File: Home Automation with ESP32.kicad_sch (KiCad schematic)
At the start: 26 parts, among them J1 Conn_01x04_Pin, J1 PR13-5V-450-1C, J2 Screw_Terminal_01x04, J3 Screw_Terminal_01x03, K1 RAYEX-L90AS, Q1 S8050, Q2 S8050, SW1 SW_Push, SW2 SW_Push, U1 ESP32-WROOM-32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

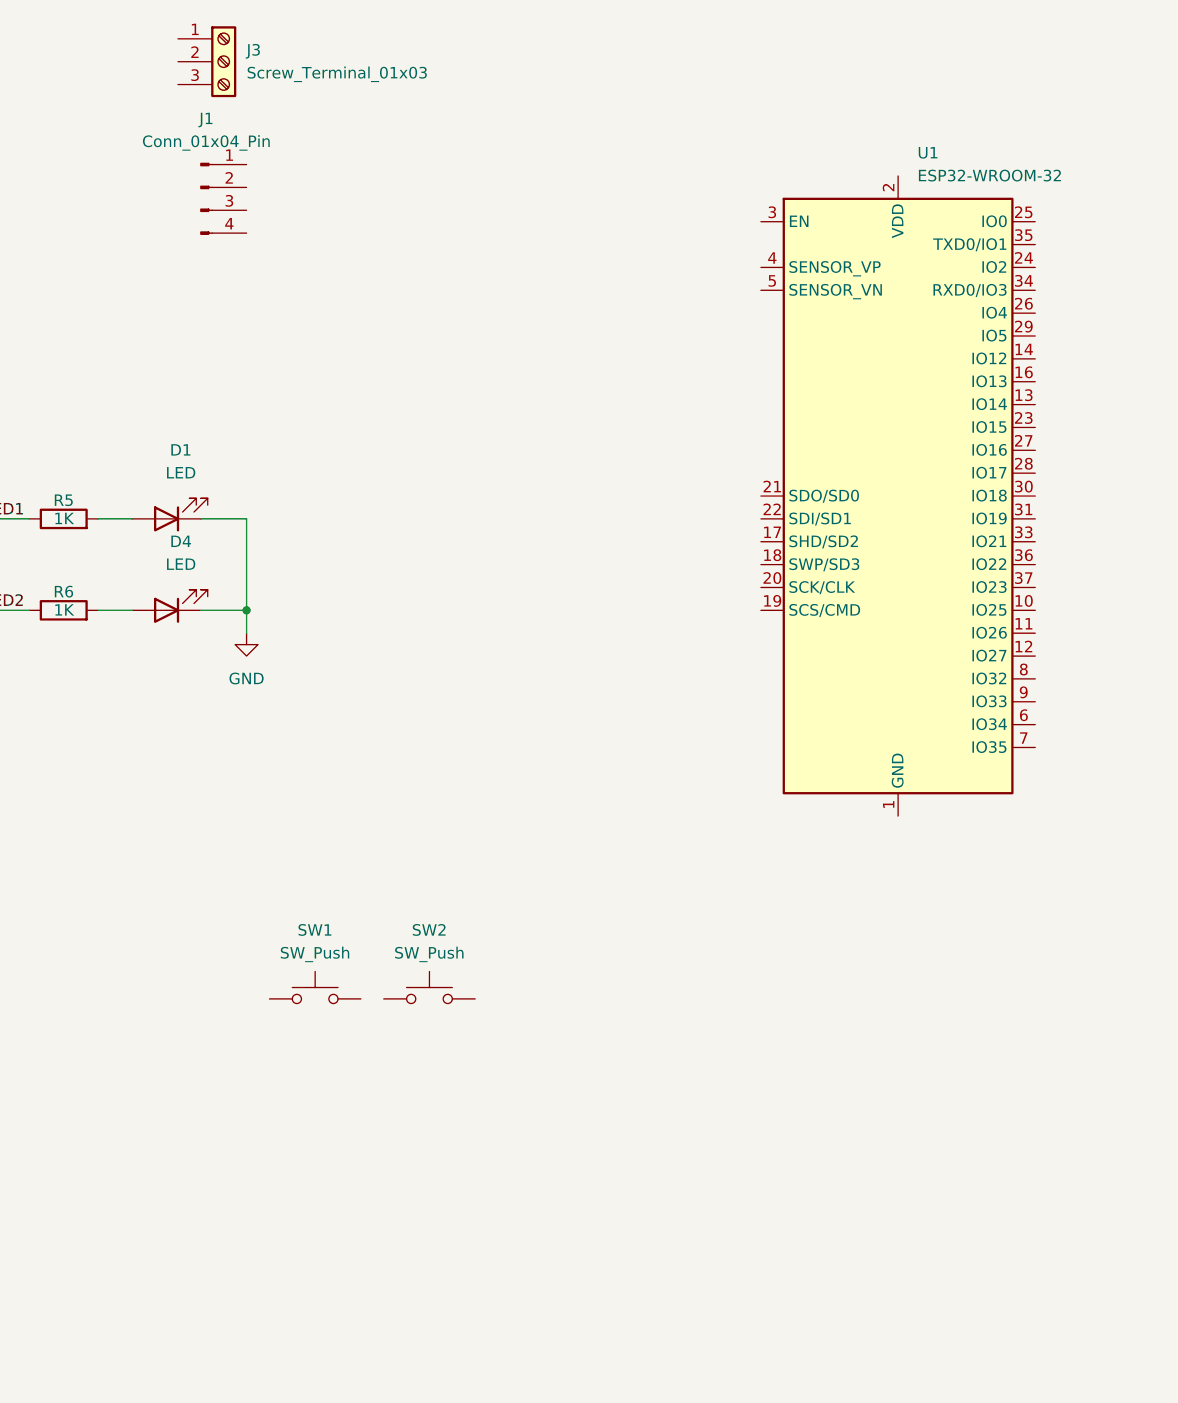
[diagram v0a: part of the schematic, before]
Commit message: Schematic Connection completed for Switches
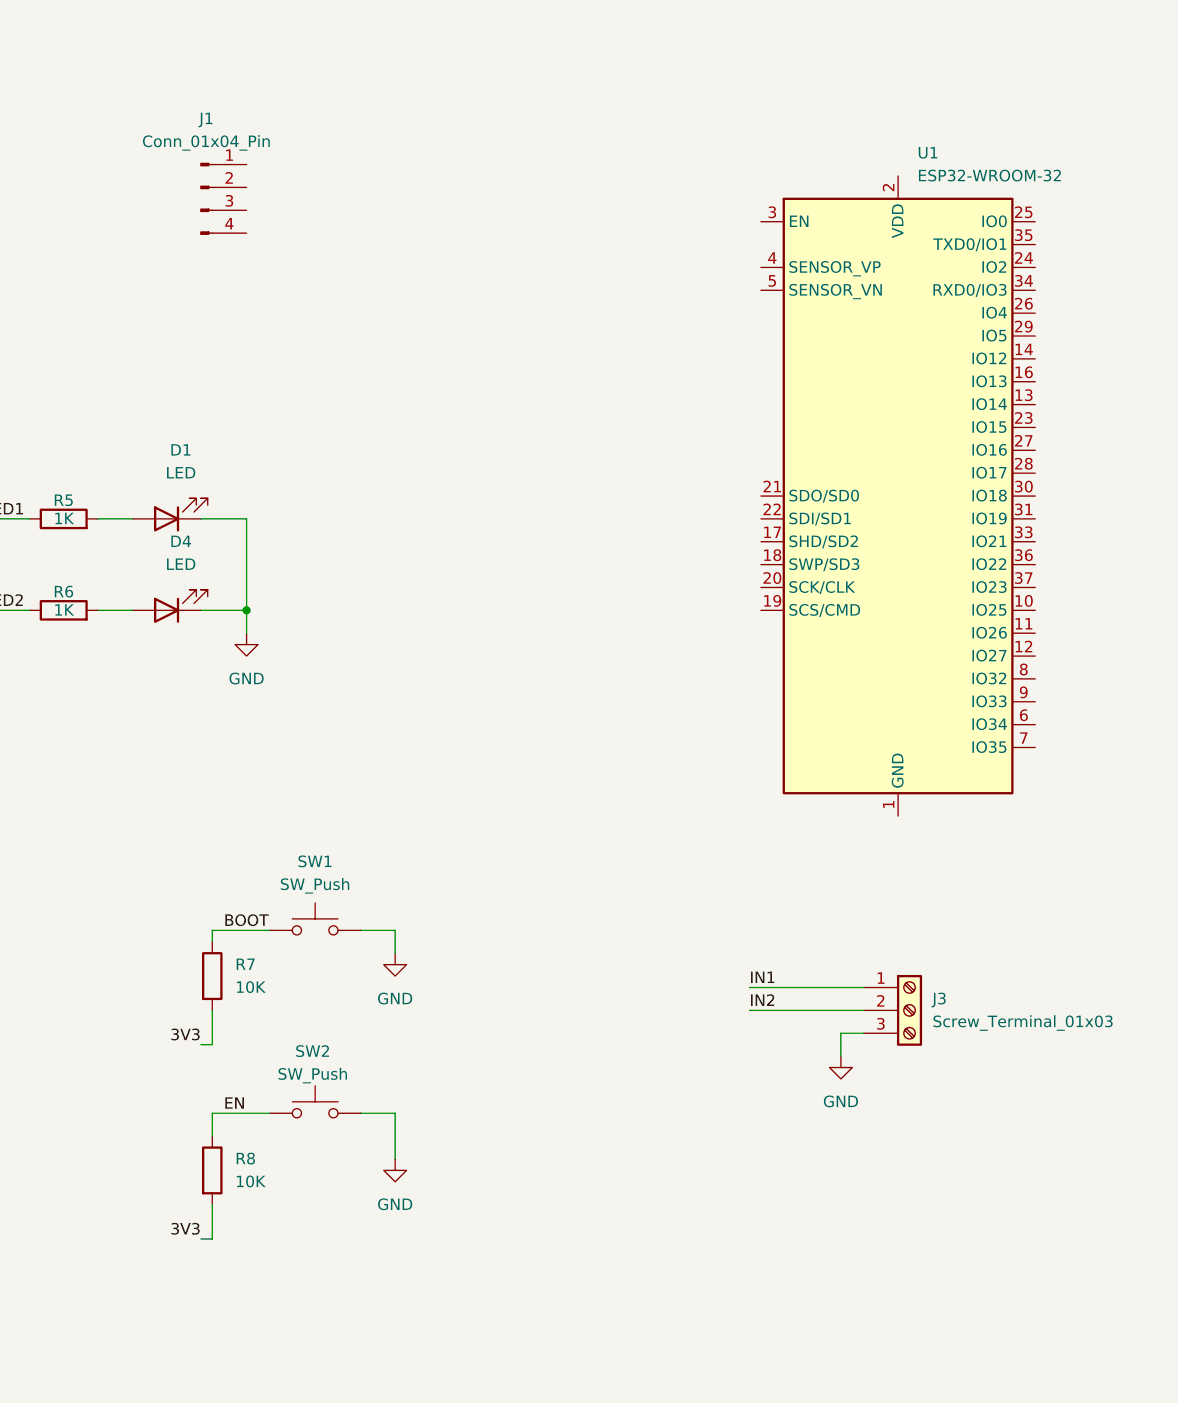
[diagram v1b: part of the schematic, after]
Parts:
- added R7, R8: 10K, symbol Device:R
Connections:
- net 3V3: now also R7.2, R8.2
- net GND: now also J3.3 (Pin_3), SW1.2, SW2.2
- net BOOT: now reaches SW1.1
- net BOOT: now also R7.1
- net EN: now reaches SW2.1
- net EN: now also R8.1
- net IN1: now reaches J3.1 (Pin_1)
- net IN2: now reaches J3.2 (Pin_2)
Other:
- moved on the sheet: J3, SW1, SW2

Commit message: Schematic Connection completed for UART
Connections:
- net 3V3: now also J1.4 (Pin_4)
- net GND: now also J1.3 (Pin_3)
- net TXD: now reaches J1.1 (Pin_1)
- net RXD: now reaches J1.2 (Pin_2)
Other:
- moved on the sheet: J1
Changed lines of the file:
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@@
+	(wire
+		(pts
+			(xy 148.59 36.83) (xy 163.83 36.83)
+		)
+		(stroke
+			(width 0)
+			(type default)
+		)
+	)
 	(wire
 		(pts
@@
 	(wire
 		(pts
+			(xy 148.59 29.21) (xy 163.83 29.21)
+		)
+		(stroke
+			(width 0)
+			(type default)
+		)
+	)
+	(wire
+		(pts
 			(xy 91.44 125.73) (xy 83.82 125.73)
 		)
@@
 	(wire
 		(pts
+			(xy 148.59 34.29) (xy 163.83 34.29)
+		)
+		(stroke
+			(width 0)
+			(type default)
+		)
+	)
+	(wire
+		(pts
 			(xy 26.67 46.99) (xy 35.56 46.99)
 		)
@@
 	(wire
 		(pts
+			(xy 143.51 31.75) (xy 163.83 31.75)
+		)
+		(stroke
+			(width 0)
+			(type default)
+		)
+	)
+	(wire
+		(pts
 			(xy 109.22 166.37) (xy 111.76 166.37)
 		)
@@
 		(pts
 			(xy 107.95 41.91) (xy 113.03 41.91)
+		)
+		(stroke
+			(width 0)
+			(type default)
+		)
+	)
+	(wire
+		(pts
+			(xy 143.51 31.75) (xy 143.51 33.02)
 		)
 		(stroke
@@
 		)
 	)
+	(label "3V3"
+		(at 148.59 29.21 0)
+		(effects
+			(font
+				(size 1.27 1.27)
+			)
+			(justify left bottom)
+		)
+	)
 	(label "P"
 		(at 67.31 177.8 180)
@@
 		)
 	)
+	(label "RXD"
+		(at 148.59 34.29 0)
+		(effects
+			(font
+				(size 1.27 1.27)
+			)
+			(justify left bottom)
+		)
+	)
 	(label "LED1"
 		(at 144.78 71.12 0)
+		(effects
+			(font
+				(size 1.27 1.27)
+			)
+			(justify left bottom)
+		)
+	)
+	(label "TXD"
+		(at 148.59 36.83 0)
 		(effects
 			(font
@@
 	(symbol
 		(lib_id "Connector:Conn_01x04_Pin")
-		(at 168.91 34.29 0)
+		(at 168.91 34.29 180)
 		(unit 1)
 		(exclude_from_sim no)
@@
 		(fields_autoplaced yes)
 		(property "Reference" "J1"
-			(at 169.545 26.67 0)
-			(effects
-				(font
-					(size 1.27 1.27)
-				)
+			(at 170.18 31.7499 0)
+			(effects
+				(font
+					(size 1.27 1.27)
+				)
+				(justify right)
 			)
 		)
 		(property "Value" "Conn_01x04_Pin"
-			(at 169.545 29.21 0)
-			(effects
-				(font
-					(size 1.27 1.27)
-				)
+			(at 170.18 34.2899 0)
+			(effects
+				(font
+					(size 1.27 1.27)
+				)
+				(justify right)
 			)
 		)
@@
 					(unit 1)
 				)
+			)
+		)
+	)
+	(symbol
+		(lib_id "power:GND")
+		(at 143.51 33.02 0)
+		(unit 1)
+		(exclude_from_sim no)
+		(in_bom yes)
+		(on_board yes)
+		(dnp no)
+		(fields_autoplaced yes)
+		(property "Reference" "#PWR012"
+			(at 143.51 39.37 0)
+			(effects
+				(font
+					(size 1.27 1.27)
+				)
+				(hide yes)
+			)
+		)
+		(property "Value" "GND"
+			(at 143.51 38.1 0)
+			(effects
+				(font
+					(size 1.27 1.27)
+				)
+			)
+		)
+		(property "Footprint" ""
+			(at 143.51 33.02 0)
+			(effects
+				(font
+					(size 1.27 1.27)
+				)
+				(hide yes)
+			)
+		)
+		(property "Datasheet" ""
+			(at 143.51 33.02 0)
+			(effects
+				(font
+					(size 1.27 1.27)
+				)
+				(hide yes)
+			)
+		)
+		(property "Description" "Power symbol creates a global label with name \"GND\" , ground"
+			(at 143.51 33.02 0)
+			(effects
+				(font
+					(size 1.27 1.27)
+				)
+				(hide yes)
+			)
+		)
+		(pin "1"
+		)
+		(instances
+			(project ""
+				(path "/7438dd54-9f08-4599-aef6-4a86e3e5147b"
+					(reference "#PWR012")
+					(unit 1)
+				)

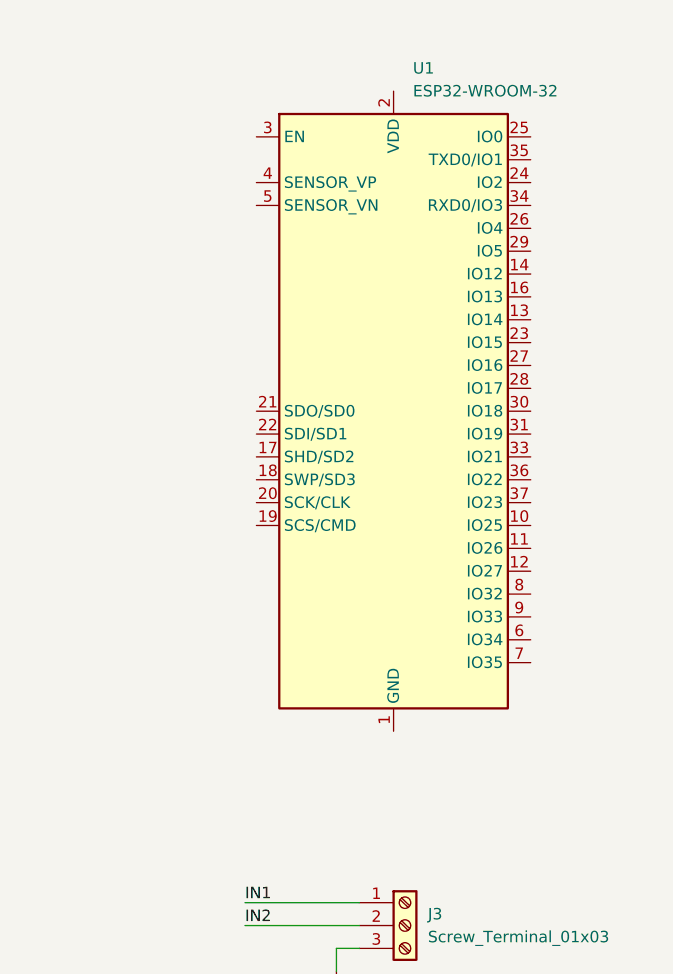
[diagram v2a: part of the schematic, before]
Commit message: Schematic Connection completed for ESP-32
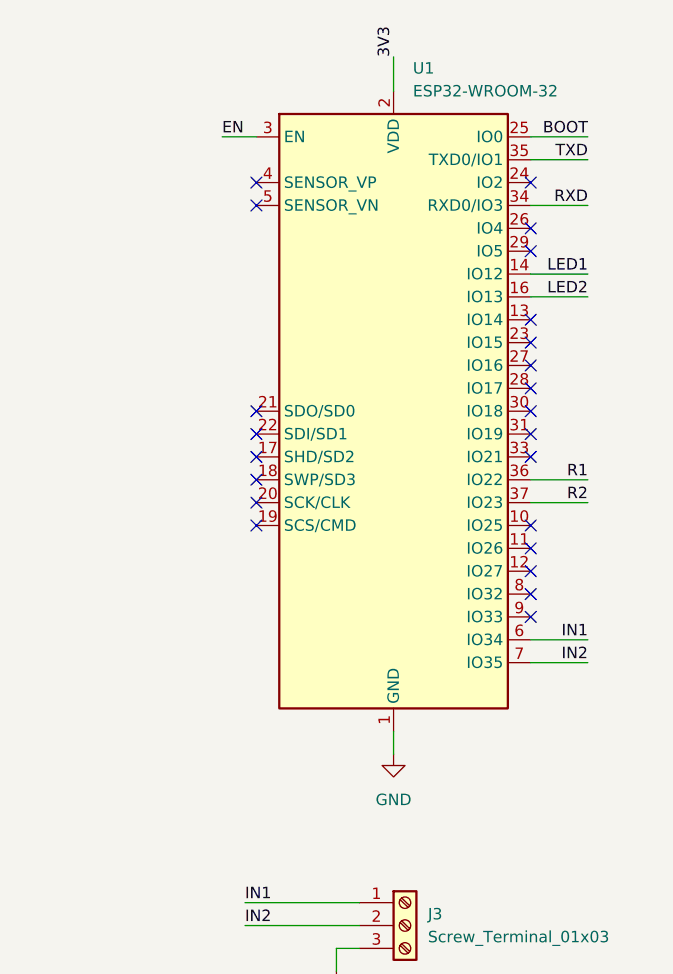
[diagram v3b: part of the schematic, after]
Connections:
- net 3V3: now also U1.2 (VDD)
- net BOOT: now also U1.25 (IO0)
- net EN: now also U1.3 (EN)
- net GND: now also U1.1 (GND), U1.15 (GND), U1.38 (GND), U1.39 (GND)
- net IN1: now also U1.6 (IO34)
- net IN2: now also U1.7 (IO35)
- net LED1: now also U1.14 (IO12)
- net LED2: now also U1.16 (IO13)
- net R1: now also U1.36 (IO22)
- net R2: now also U1.37 (IO23)
- net RXD: now also U1.34 (RXD0/IO3)
- net TXD: now also U1.35 (TXD0/IO1)
- no-connect marks 0 -> 23

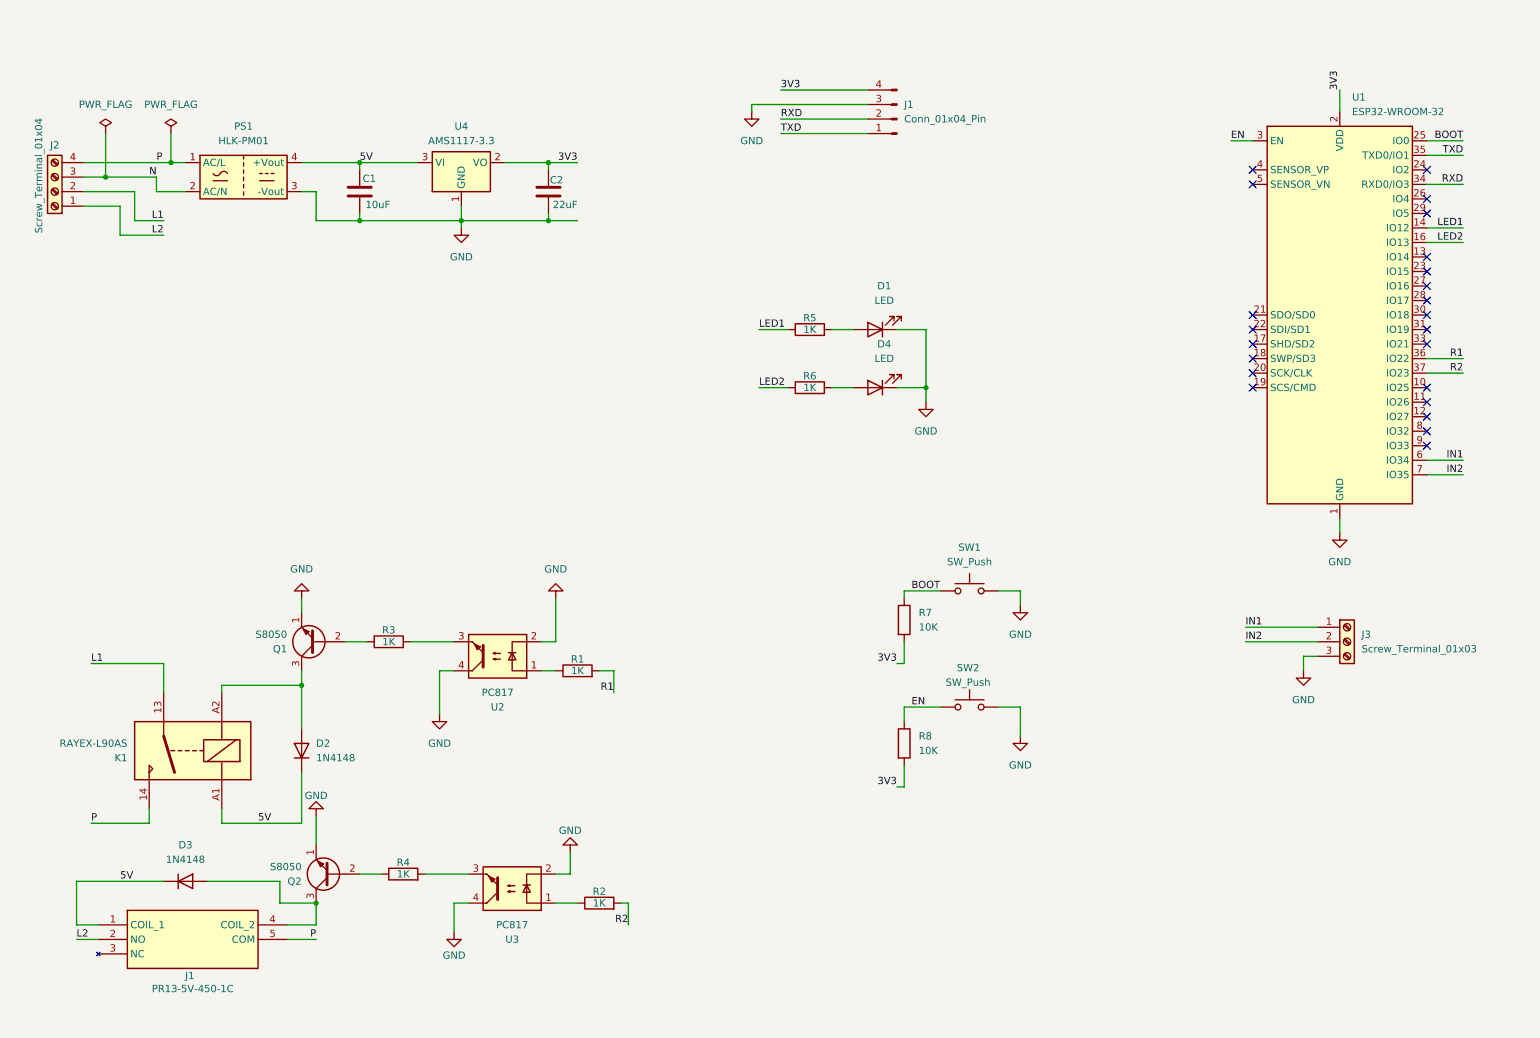
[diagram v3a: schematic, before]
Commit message: Placed the Mounting_Pad in Schematic
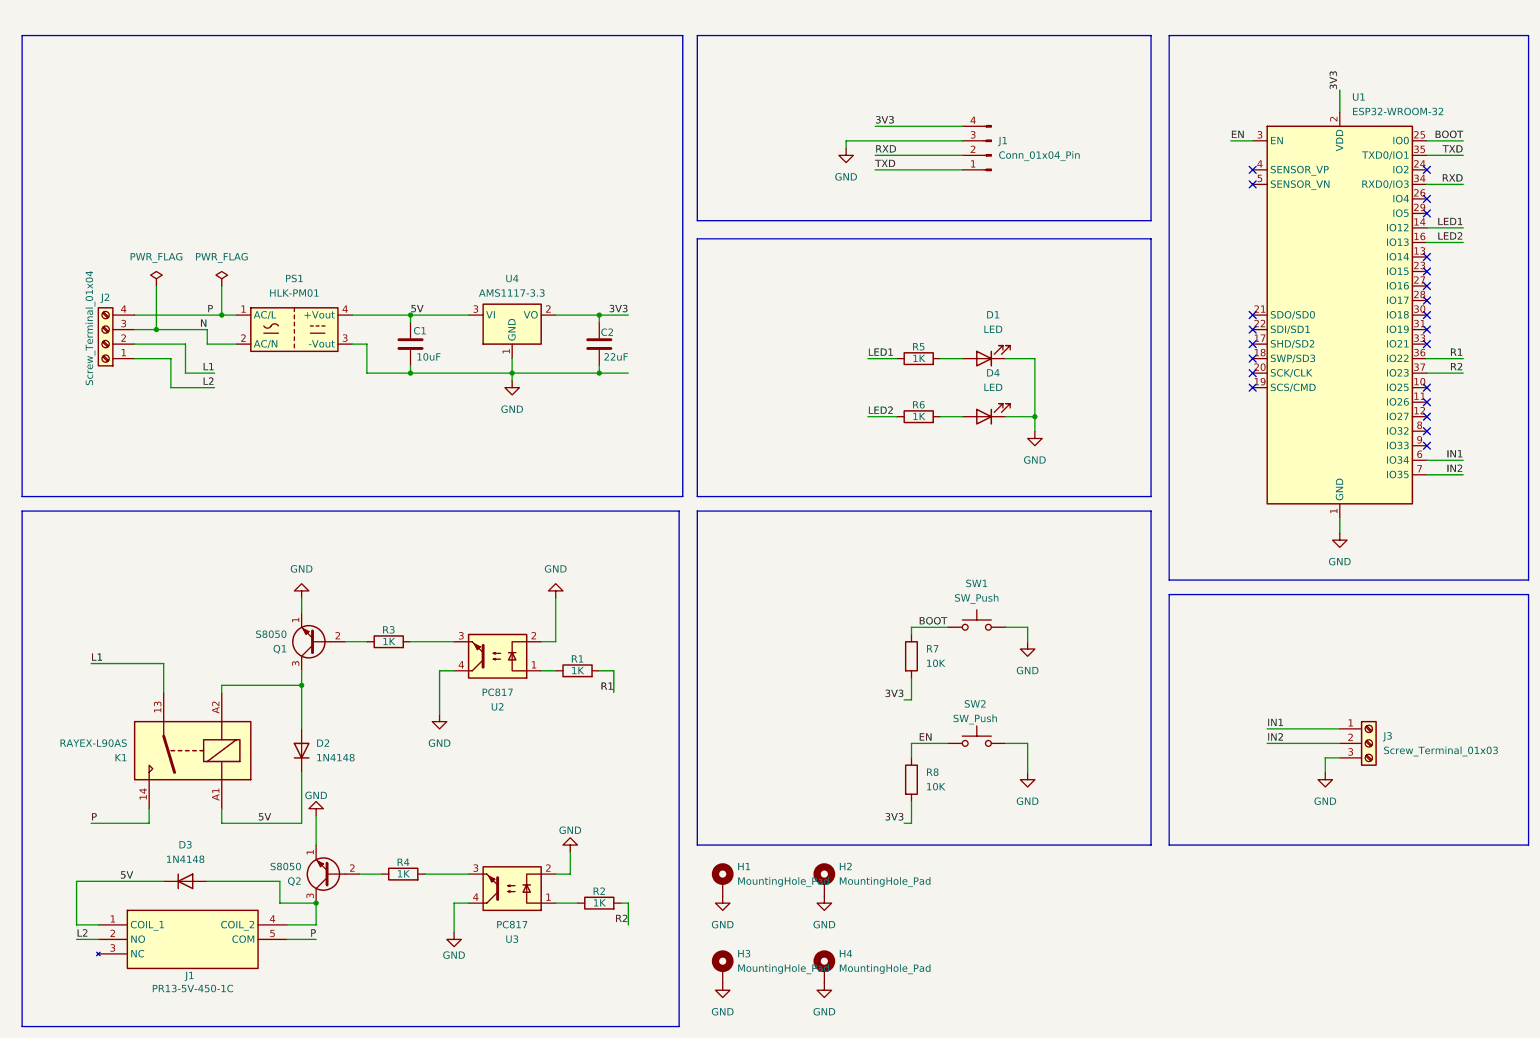
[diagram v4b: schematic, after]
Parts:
- added H1, H2, H3, H4: MountingHole_Pad, symbol Mechanical:MountingHole_Pad
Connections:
- net GND: now also H1.1, H2.1, H3.1, H4.1
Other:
- moved on the sheet: C1, C2, D1, D4, J1, J2, J3, PS1, R5, R6, R7, R8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

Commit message: Naming in Schematic is Completed
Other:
- note added: "LED's"
- note added: "MCU"
- note added: "POWER SUPPLY"
- note added: "RELAY's"
- note added: "RESET & BOOT"
- note added: "SWITCHES"
- note added: "UART"
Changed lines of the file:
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@@
+		)
+	)
+	(text "LED's"
+		(exclude_from_sim no)
+		(at 146.05 62.23 0)
+		(effects
+			(font
+				(face "KiCad Font")
+				(size 5 5)
+				(thickness 1)
+				(bold yes)
+			)
+		)
+	)
+	(text "RELAY's"
+		(exclude_from_sim no)
+		(at 34.036 108.966 0)
+		(effects
+			(font
+				(face "KiCad Font")
+				(size 5 5)
+				(thickness 1)
+				(bold yes)
+			)
+		)
+	)
+	(text "UART"
+		(exclude_from_sim no)
+		(at 144.78 27.94 0)
+		(effects
+			(font
+				(face "KiCad Font")
+				(size 5 5)
+				(thickness 1)
+				(bold yes)
+			)
+		)
+	)
+	(text "RESET & BOOT"
+		(exclude_from_sim no)
+		(at 164.084 109.22 0)
+		(effects
+			(font
+				(face "KiCad Font")
+				(size 5 5)
+				(thickness 1)
+				(bold yes)
+			)
+		)
+	)
+	(text "SWITCHES"
+		(exclude_from_sim no)
+		(at 236.728 123.952 0)
+		(effects
+			(font
+				(face "KiCad Font")
+				(size 5 5)
+				(thickness 1)
+				(bold yes)
+			)
+		)
+	)
+	(text "MCU"
+		(exclude_from_sim no)
+		(at 226.822 25.908 0)
+		(effects
+			(font
+				(face "KiCad Font")
+				(size 5 5)
+				(thickness 1)
+				(bold yes)
+			)
+		)
+	)
+	(text "POWER SUPPLY"
+		(exclude_from_sim no)
+		(at 48.006 27.686 0)
+		(effects
+			(font
+				(face "KiCad Font")
+				(size 5 5)
+				(thickness 1.4)
+				(bold yes)
+			)
 		)
 	)
